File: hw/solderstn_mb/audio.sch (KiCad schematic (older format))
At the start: 30 parts, among them J2103 CES-30207-158L120-67_Molex-Pi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, J2104 CES-703116-28PM_JST-conn, J2105 CES-30207-158L120-67_Molex-Pi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, J2106 CES-703116-28PM_JST-conn, U2102 TS4990IDT, U2103 TS4990IDT

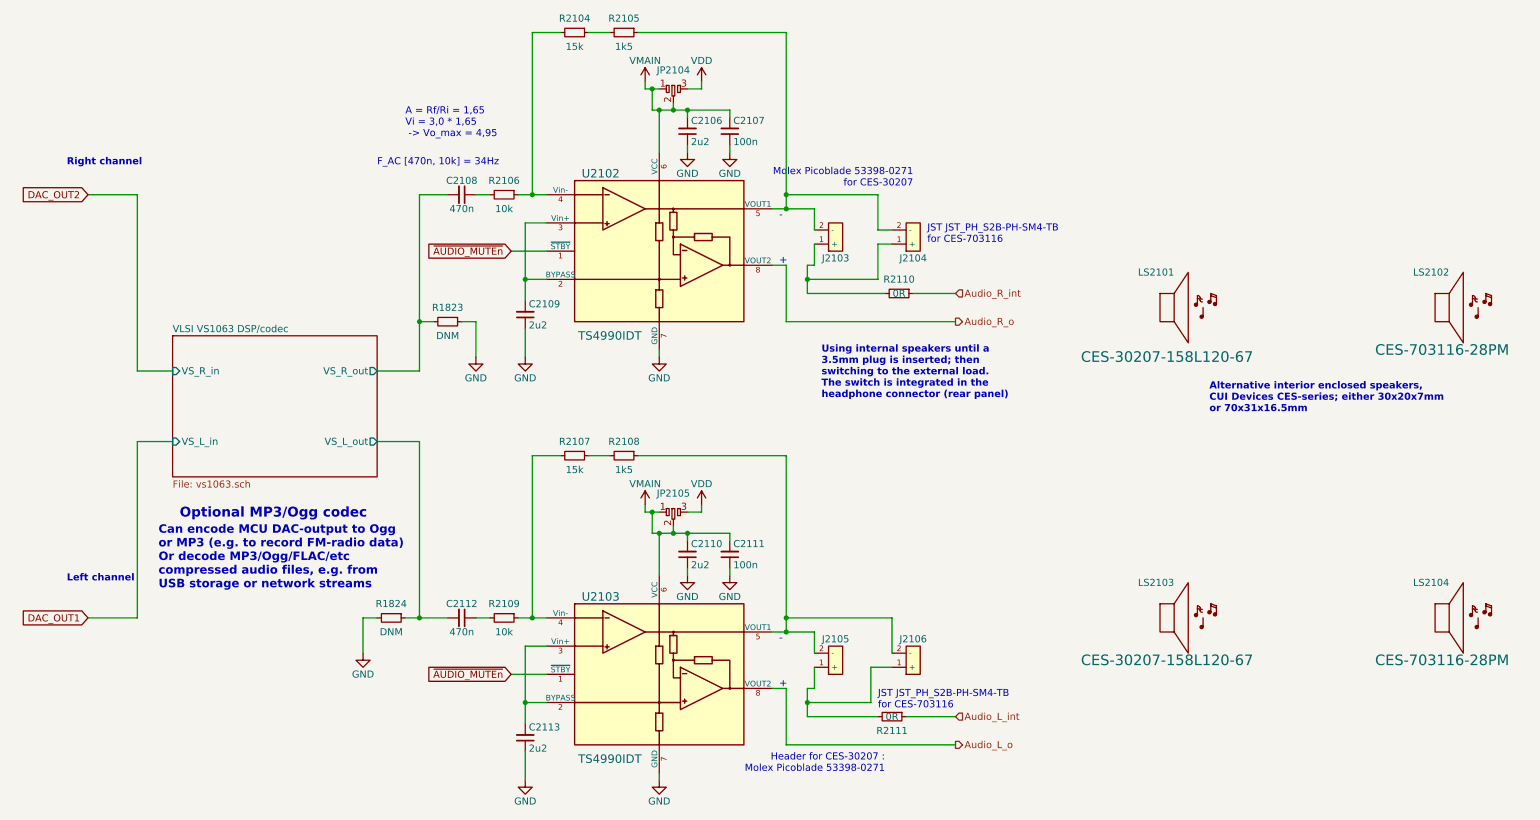
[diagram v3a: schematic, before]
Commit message: Reannotate entire schematic; add temp.extra SMA-conn to eval alternative FMI placement
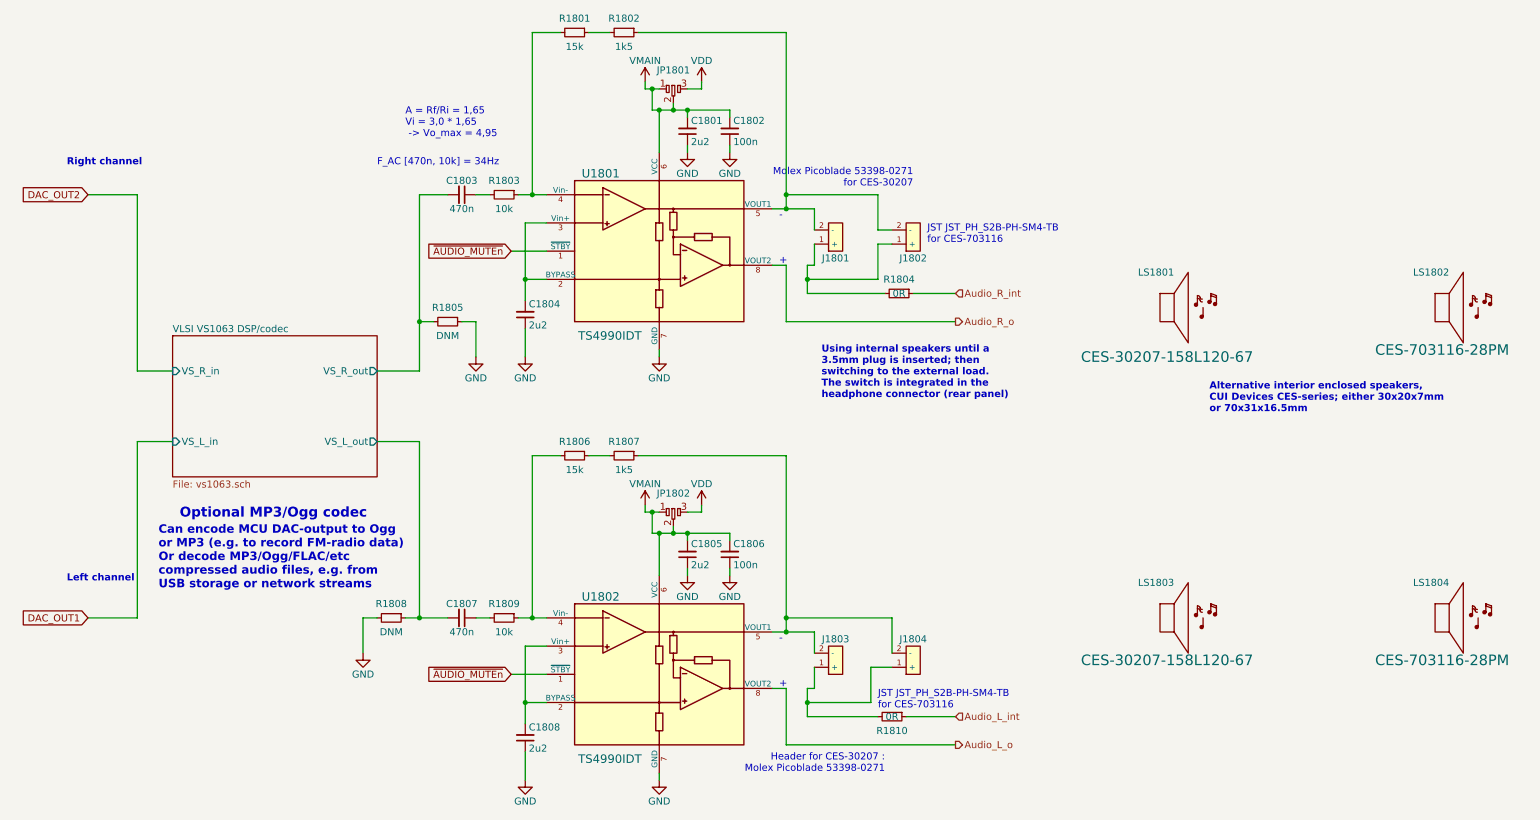
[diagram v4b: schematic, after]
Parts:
- renumbered C2106 to C1801, C2107 to C1802, C2108 to C1803, C2109 to C1804, C2110 to C1805, C2111 to C1806, C2112 to C1807, C2113 to C1808, J2103 to J1801, J2104 to J1802, J2105 to J1803, J2106 to J1804, JP2104 to JP1801, JP2105 to JP1802, LS2101 to LS1801, LS2102 to LS1802, LS2103 to LS1803, LS2104 to LS1804, R2104 to R1801, R2105 to R1802, R2106 to R1803, R2110 to R1804, R1823 to R1805, R2107 to R1806, R2108 to R1807, R1824 to R1808, R2109 to R1809, R2111 to R1810, U2102 to U1801, U2103 to U1802

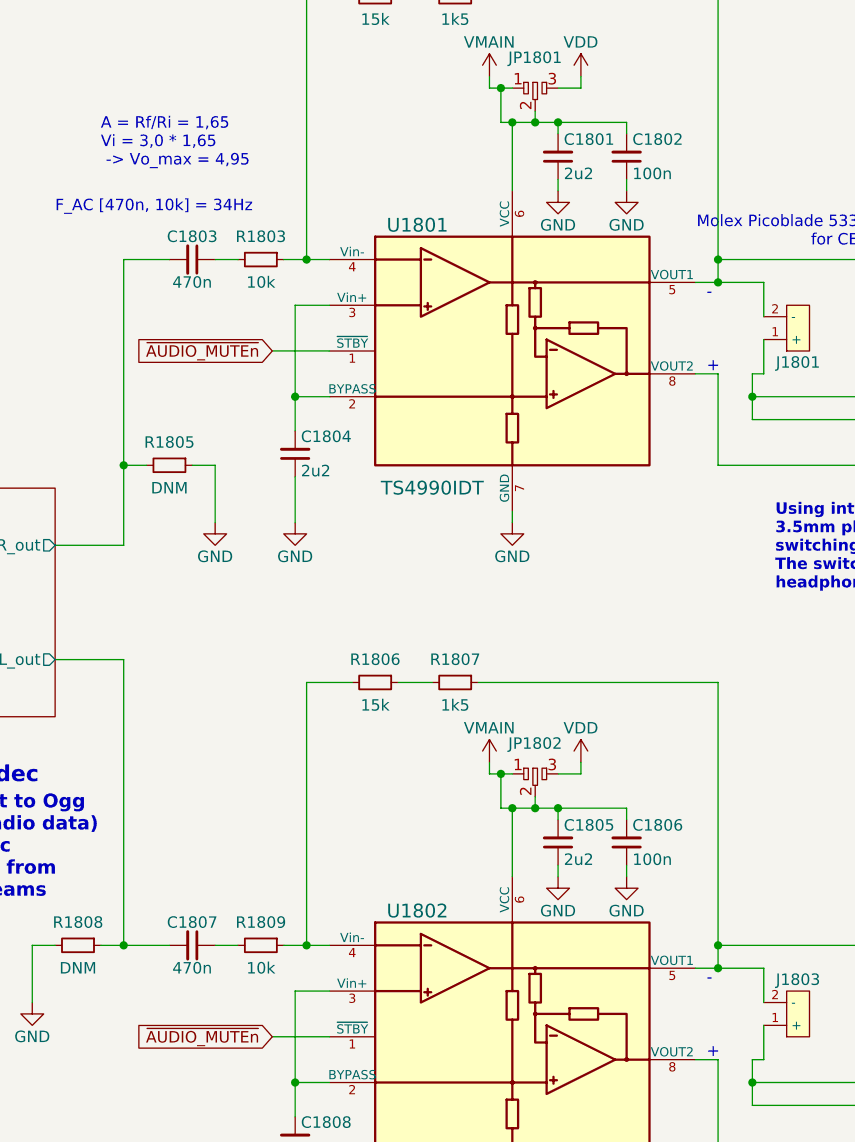
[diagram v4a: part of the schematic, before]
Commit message: MB: major update of footprints, LCSC part numbers and Basic/Extended library indicator, for _most_ of the BoM. (Also removed JP1101/JP1102, bypass jmprs)
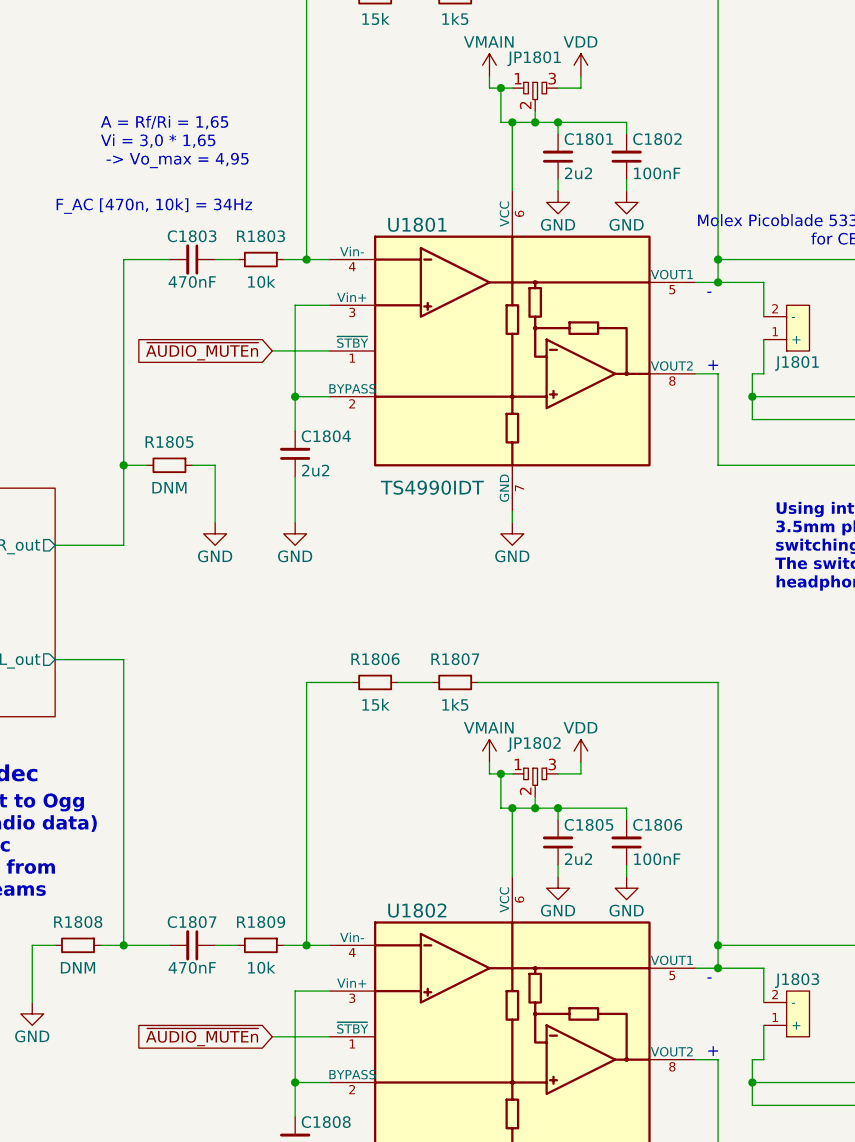
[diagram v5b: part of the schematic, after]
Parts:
- C1801, C1804, C1805, C1808: JLC_part (none) -> Basic; LCSC (none) -> C23630
- C1802, C1806: value 100n -> 100nF; footprint Capacitor_SMD:C_0603_1608Metric -> Capacitor_SMD:C_0402_1005Metric; JLC_part (none) -> Basic; LCSC (none) -> C1525
- C1803, C1807: value 470n -> 470nF; footprint Capacitor_SMD:C_0603_1608Metric -> Capacitor_SMD:C_0402_1005Metric; JLC_part (none) -> Basic; LCSC (none) -> C47339
- R1801, R1806: footprint Resistor_SMD:R_0603_1608Metric -> Resistor_SMD:R_0402_1005Metric; JLC_part (none) -> Basic; LCSC (none) -> C25756
- R1802, R1807: footprint Resistor_SMD:R_0603_1608Metric -> Resistor_SMD:R_0402_1005Metric; JLC_part (none) -> Basic; LCSC (none) -> C25867
- R1803, R1809: footprint Resistor_SMD:R_0603_1608Metric -> Resistor_SMD:R_0402_1005Metric; JLC_part (none) -> Basic; LCSC (none) -> C25744
- R1804, R1810: JLC_part (none) -> Basic; LCSC (none) -> C17888
- R1805, R1808: footprint Resistor_SMD:R_0603_1608Metric -> Resistor_SMD:R_0402_1005Metric
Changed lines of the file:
@@
 P 3600 2100
 F 0 "C1803" V 3700 2100 50  0000 C CNN
-F 1 "470n" V 3500 2100 50  0000 C CNN
-F 2 "Capacitor_SMD:C_0603_1608Metric" H 3600 2100 50  0001 C CNN
+F 1 "470nF" V 3500 2100 50  0000 C CNN
+F 2 "Capacitor_SMD:C_0402_1005Metric" H 3600 2100 50  0001 C CNN
 F 3 "~" H 3600 2100 50  0001 C CNN
+F 4 "Basic" H 3600 2100 50  0001 C CNN "JLC_part"
+F 5 "C47339" H 3600 2100 50  0001 C CNN "LCSC"
 	1    3600 2100
 	0    1    -1   0
@@
 F 0 "R1801" V 4300 950 50  0000 C CNN
 F 1 "15k" V 4500 950 50  0000 C CNN
-F 2 "Resistor_SMD:R_0603_1608Metric" H 4400 950 50  0001 C CNN
+F 2 "Resistor_SMD:R_0402_1005Metric" H 4400 950 50  0001 C CNN
 F 3 "~" H 4400 950 50  0001 C CNN
+F 4 "Basic" H 4400 950 50  0001 C CNN "JLC_part"
+F 5 "C25756" H 4400 950 50  0001 C CNN "LCSC"
 	1    4400 950
 	0    1    1    0
@@
 F 0 "R1802" V 4650 950 50  0000 C CNN
 F 1 "1k5" V 4850 950 50  0000 C CNN
-F 2 "Resistor_SMD:R_0603_1608Metric" H 4750 950 50  0001 C CNN
+F 2 "Resistor_SMD:R_0402_1005Metric" H 4750 950 50  0001 C CNN
 F 3 "~" H 4750 950 50  0001 C CNN
+F 4 "Basic" H 4750 950 50  0001 C CNN "JLC_part"
+F 5 "C25867" H 4750 950 50  0001 C CNN "LCSC"
 	1    4750 950
 	0    1    1    0
@@
 F 0 "R1803" V 3800 2100 50  0000 C CNN
 F 1 "10k" V 4000 2100 50  0000 C CNN
-F 2 "Resistor_SMD:R_0603_1608Metric" H 3900 2100 50  0001 C CNN
+F 2 "Resistor_SMD:R_0402_1005Metric" H 3900 2100 50  0001 C CNN
 F 3 "~" H 3900 2100 50  0001 C CNN
+F 4 "Basic" H 3900 2100 50  0001 C CNN "JLC_part"
+F 5 "C25744" H 3900 2100 50  0001 C CNN "LCSC"
 	1    3900 2100
 	0    1    1    0
@@
 F 2 "Capacitor_SMD:C_0603_1608Metric" H 4050 2950 50  0001 C CNN
 F 3 "~" H 4050 2950 50  0001 C CNN
+F 4 "Basic" H 4050 2950 50  0001 C CNN "JLC_part"
+F 5 "C23630" H 4050 2950 50  0001 C CNN "LCSC"
 	1    4050 2950
 	1    0    0    1
@@
 F 2 "Capacitor_SMD:C_0603_1608Metric" H 5200 1650 50  0001 C CNN
 F 3 "~" H 5200 1650 50  0001 C CNN
+F 4 "Basic" H 5200 1650 50  0001 C CNN "JLC_part"
+F 5 "C23630" H 5200 1650 50  0001 C CNN "LCSC"
 	1    5200 1650
 	1    0    0    1
@@
 P 3600 5100
 F 0 "C1807" V 3700 5100 50  0000 C CNN
-F 1 "470n" V 3500 5100 50  0000 C CNN
-F 2 "Capacitor_SMD:C_0603_1608Metric" H 3600 5100 50  0001 C CNN
+F 1 "470nF" V 3500 5100 50  0000 C CNN
+F 2 "Capacitor_SMD:C_0402_1005Metric" H 3600 5100 50  0001 C CNN
 F 3 "~" H 3600 5100 50  0001 C CNN
+F 4 "Basic" H 3600 5100 50  0001 C CNN "JLC_part"
+F 5 "C47339" H 3600 5100 50  0001 C CNN "LCSC"
 	1    3600 5100
 	0    1    -1   0
@@
 F 0 "R1806" V 4300 3950 50  0000 C CNN
 F 1 "15k" V 4500 3950 50  0000 C CNN
-F 2 "Resistor_SMD:R_0603_1608Metric" H 4400 3950 50  0001 C CNN
+F 2 "Resistor_SMD:R_0402_1005Metric" H 4400 3950 50  0001 C CNN
 F 3 "~" H 4400 3950 50  0001 C CNN
+F 4 "Basic" H 4400 3950 50  0001 C CNN "JLC_part"
+F 5 "C25756" H 4400 3950 50  0001 C CNN "LCSC"
 	1    4400 3950
 	0    1    1    0
@@
 F 0 "R1807" V 4650 3950 50  0000 C CNN
 F 1 "1k5" V 4850 3950 50  0000 C CNN
-F 2 "Resistor_SMD:R_0603_1608Metric" H 4750 3950 50  0001 C CNN
+F 2 "Resistor_SMD:R_0402_1005Metric" H 4750 3950 50  0001 C CNN
 F 3 "~" H 4750 3950 50  0001 C CNN
+F 4 "Basic" H 4750 3950 50  0001 C CNN "JLC_part"
+F 5 "C25867" H 4750 3950 50  0001 C CNN "LCSC"
 	1    4750 3950
 	0    1    1    0
@@
 F 0 "R1809" V 3800 5100 50  0000 C CNN
 F 1 "10k" V 4000 5100 50  0000 C CNN
-F 2 "Resistor_SMD:R_0603_1608Metric" H 3900 5100 50  0001 C CNN
+F 2 "Resistor_SMD:R_0402_1005Metric" H 3900 5100 50  0001 C CNN
 F 3 "~" H 3900 5100 50  0001 C CNN
+F 4 "Basic" H 3900 5100 50  0001 C CNN "JLC_part"
+F 5 "C25744" H 3900 5100 50  0001 C CNN "LCSC"
 	1    3900 5100
 	0    1    1    0
@@
 F 2 "Capacitor_SMD:C_0603_1608Metric" H 4050 5950 50  0001 C CNN
 F 3 "~" H 4050 5950 50  0001 C CNN
+F 4 "Basic" H 4050 5950 50  0001 C CNN "JLC_part"
+F 5 "C23630" H 4050 5950 50  0001 C CNN "LCSC"
 	1    4050 5950
 	1    0    0    1
@@
 F 2 "Capacitor_SMD:C_0603_1608Metric" H 5200 4650 50  0001 C CNN
 F 3 "~" H 5200 4650 50  0001 C CNN
+F 4 "Basic" H 5200 4650 50  0001 C CNN "JLC_part"
+F 5 "C23630" H 5200 4650 50  0001 C CNN "LCSC"
 	1    5200 4650
 	1    0    0    1
@@
 P 5500 1650
 F 0 "C1802" H 5525 1575 50  0000 L CNN
-F 1 "100n" H 5525 1725 50  0000 L CNN
-F 2 "Capacitor_SMD:C_0603_1608Metric" H 5500 1650 50  0001 C CNN
+F 1 "100nF" H 5525 1725 50  0000 L CNN
+F 2 "Capacitor_SMD:C_0402_1005Metric" H 5500 1650 50  0001 C CNN
 F 3 "~" H 5500 1650 50  0001 C CNN
+F 4 "Basic" H 5500 1650 50  0001 C CNN "JLC_part"
+F 5 "C1525" H 5500 1650 50  0001 C CNN "LCSC"
 	1    5500 1650
 	1    0    0    1
@@
 P 5500 4650
 F 0 "C1806" H 5525 4575 50  0000 L CNN
-F 1 "100n" H 5525 4725 50  0000 L CNN
-F 2 "Capacitor_SMD:C_0603_1608Metric" H 5500 4650 50  0001 C CNN
+F 1 "100nF" H 5525 4725 50  0000 L CNN
+F 2 "Capacitor_SMD:C_0402_1005Metric" H 5500 4650 50  0001 C CNN
 F 3 "~" H 5500 4650 50  0001 C CNN
+F 4 "Basic" H 5500 4650 50  0001 C CNN "JLC_part"
+F 5 "C1525" H 5500 4650 50  0001 C CNN "LCSC"
 	1    5500 4650
 	1    0    0    1
@@
 F 2 "Resistor_SMD:R_1206_3216Metric" H 6700 2800 50  0001 C CNN
 F 3 "~" H 6700 2800 50  0001 C CNN
+F 4 "Basic" H 6700 2800 50  0001 C CNN "JLC_part"
+F 5 "C17888" H 6700 2800 50  0001 C CNN "LCSC"
 	1    6700 2800
 	0    1    1    0
@@
 F 2 "Resistor_SMD:R_1206_3216Metric" H 6650 5800 50  0001 C CNN
 F 3 "~" H 6650 5800 50  0001 C CNN
+F 4 "Basic" H 6650 5800 50  0001 C CNN "JLC_part"
+F 5 "C17888" H 6650 5800 50  0001 C CNN "LCSC"
 	1    6650 5800
 	0    1    1    0
@@
 F 0 "R1805" V 3400 3000 50  0000 C CNN
 F 1 "DNM" V 3600 3000 50  0000 C CNN
-F 2 "Resistor_SMD:R_0603_1608Metric" H 3500 3000 50  0001 C CNN
+F 2 "Resistor_SMD:R_0402_1005Metric" H 3500 3000 50  0001 C CNN
 F 3 "~" H 3500 3000 50  0001 C CNN
 	1    3500 3000
@@
 F 0 "R1808" V 3000 5100 50  0000 C CNN
 F 1 "DNM" V 3200 5100 50  0000 C CNN
-F 2 "Resistor_SMD:R_0603_1608Metric" H 3100 5100 50  0001 C CNN
+F 2 "Resistor_SMD:R_0402_1005Metric" H 3100 5100 50  0001 C CNN
 F 3 "~" H 3100 5100 50  0001 C CNN
 	1    3100 5100
